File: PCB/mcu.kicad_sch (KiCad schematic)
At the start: 16 parts, among them J3 USB_A, SW1 SW_Push, SW2 SW_Push, SW3 SW_Push, SW4 SW_Push, U3 COM-09032, Y1 Crystal_GND24

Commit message: pls work
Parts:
- added C85, C86, C87, C88, C89, C90, C91: 100n, symbol Device:C
- added C92: 10u, symbol Device:C_Polarized_US
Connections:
- net +3.3V: now also C85.1, C86.1, C87.1, C88.1, C89.1, C90.1, C91.1, C92.1
- net GND: now also C85.2, C86.2, C87.2, C88.2, C89.2, C90.2, C91.2, C92.2

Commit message: Footprints
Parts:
- removed J3: USB_A, symbol Connector:USB_A
- added J6: USB1130-15-A_REVA, USB1130-15-A_REVA:GCT_USB1130-15-A_REVA, symbol USB1130-15-A_REVA:USB1130-15-A_REVA
- C20, C21, C22, C85, C86, C87, C88, C89, C90, C91, C92: footprint (none) -> Capacitor_SMD:C_0805_2012Metric_Pad1.18x1.45mm_HandSolder
- H1: footprint (none) -> efm32:QFP50P1200X1200X120-64N
- R10, R11, R12, R9: footprint (none) -> Resistor_SMD:R_0805_2012Metric_Pad1.20x1.40mm_HandSolder
- SW1, SW2, SW3, SW4: footprint (none) -> button:K12PBK15N
- U3: footprint COM-09032:XDCR_COM-09032 -> joystick:XDCR_COM-09032
- Y1: footprint (none) -> ECS-3953M-400-BN-TR:OSC_ECS-3953M-400-BN-TR
- renumbered DEBUG_HEADER to DEBUG_HEADER1
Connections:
- net 5V_IN: now also J6.1 (VCC)
- net GND: now also J6.4 (GND)
- net at H1.47 (PF10): now also J6.2 (D-)
- net at H1.48 (PF11): now also J6.3 (D+)
- new net: J6.S1 (SHIELD), J6.S2 (SHIELD)

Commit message: more
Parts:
- added R38, R39: 15, symbol Device:R
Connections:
- net +3.3VA is gone; now on net +3.3V: H1.23 (AVDD_1), H1.27 (AVDD_0)
- net 5V_IN: now also H1.52 (USB_VBUS)
- net GND: now also H1.33 (PD5), H1.34 (PD6), H1.35 (PD7), J6.S1 (SHIELD), J6.S2 (SHIELD), U3.S1 (SHIELD), U3.S2 (SHIELD), U3.S3 (SHIELD), U3.S4 (SHIELD); no longer H1.52 (USB_VBUS)
- net at J6.2 (D-): now also R38.2; no longer H1.47 (PF10)
- net at J6.3 (D+): now also R39.2; no longer H1.48 (PF11)
- net at DEBUG_HEADER1.12 (TRACECLK): no longer H1.35 (PD7)
- net at DEBUG_HEADER1.14 (TRACEDATA[0]): no longer H1.34 (PD6)
- net at DEBUG_HEADER1.16 (TRACEDATA[1]): no longer H1.31 (PD3)
- net at DEBUG_HEADER1.18 (TRACEDATA[2]): no longer H1.32 (PD4)
- net at DEBUG_HEADER1.20 (TRACEDATA[3]): no longer H1.33 (PD5)
- new net: H1.47 (PF10), R38.1
- new net: H1.48 (PF11), R39.1
- no-connect marks 6 -> 9

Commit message: schematic fixes
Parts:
- added C2: 10u?, Capacitor_SMD:C_0805_2012Metric_Pad1.18x1.45mm_HandSolder, symbol Device:C
- added C93: 1u, Capacitor_SMD:C_0805_2012Metric_Pad1.18x1.45mm_HandSolder, symbol Device:C
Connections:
- net 5V_IN: now also C2.1
- net GND: now also H1.31 (PD3), H1.32 (PD4), C2.2, C93.2; no longer H1.33 (PD5), H1.34 (PD6), H1.45 (USB_VREGI)
- net at H1.46 (USB_VREGO): now also H1.45 (USB_VREGI), C93.1
- new net done: H1.34 (PD6)
- new net program_b: H1.33 (PD5)
- no-connect marks 9 -> 8
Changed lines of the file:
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@@
   (junction (at 110.49 24.13) (diameter 0) (color 0 0 0 0)
   )
+  (junction (at 111.76 130.81) (diameter 0) (color 0 0 0 0)
+  )
   (junction (at 53.34 60.96) (diameter 0) (color 0 0 0 0)
   )
@@
   (junction (at 68.58 90.17) (diameter 0) (color 0 0 0 0)
   )
-  (junction (at 121.92 105.41) (diameter 0) (color 0 0 0 0)
+  (junction (at 121.92 77.47) (diameter 0) (color 0 0 0 0)
   )
   (junction (at 101.6 158.75) (diameter 0) (color 0 0 0 0)
@@
   (junction (at 118.745 31.75) (diameter 0) (color 0 0 0 0)
   )
+  (junction (at 128.905 80.01) (diameter 0) (color 0 0 0 0)
+  )
   (junction (at 127 31.75) (diameter 0) (color 0 0 0 0)
   )
@@
   (junction (at 57.15 60.96) (diameter 0) (color 0 0 0 0)
   )
-  (junction (at 121.92 107.95) (diameter 0) (color 0 0 0 0)
-  )
   (junction (at 49.53 74.93) (diameter 0) (color 0 0 0 0)
   )
@@
   )
   (junction (at 17.78 93.98) (diameter 0) (color 0 0 0 0)
+  )
+  (junction (at 139.7 41.91) (diameter 0) (color 0 0 0 0)
   )
   (junction (at 118.745 24.13) (diameter 0) (color 0 0 0 0)
@@
   (no_connect (at 125.73 162.56))
   (no_connect (at 201.93 90.17))
-  (no_connect (at 123.19 77.47))
   (no_connect (at 201.93 87.63))
   (no_connect (at 125.73 165.1))
   (no_connect (at 201.93 92.71))
+  (wire (pts (xy 142.875 80.01) (xy 147.32 80.01))
+    (stroke (width 0) (type default))
+  )
   (wire (pts (xy 88.9 158.75) (xy 91.44 158.75))
     (stroke (width 0) (type default))
@@
     (stroke (width 0) (type default))
   )
-  (wire (pts (xy 121.92 107.95) (xy 121.92 110.49))
-    (stroke (width 0) (type default))
-  )
   (wire (pts (xy 121.92 72.39) (xy 132.08 72.39))
     (stroke (width 0) (type default))
@@
     (stroke (width 0) (type default))
   )
-  (wire (pts (xy 111.76 130.81) (xy 111.76 133.35))
-    (stroke (width 0) (type default))
-  )
   (wire (pts (xy 36.83 80.01) (xy 36.83 114.3))
     (stroke (width 0) (type default))
   )
+  (wire (pts (xy 109.22 130.81) (xy 111.76 130.81))
+    (stroke (width 0) (type default))
+  )
   (wire (pts (xy 88.9 158.75) (xy 88.9 162.56))
     (stroke (width 0) (type default))
@@
     (stroke (width 0) (type default))
   )
+  (wire (pts (xy 121.92 77.47) (xy 128.905 77.47))
+    (stroke (width 0) (type default))
+  )
   (wire (pts (xy 147.32 63.5) (xy 149.86 63.5))
     (stroke (width 0) (type default))
@@
     (stroke (width 0) (type default))
   )
-  (wire (pts (xy 114.3 130.81) (xy 205.74 130.81))
-    (stroke (width 0) (type default))
-  )
   (wire (pts (xy 132.08 72.39) (xy 132.08 66.04))
     (stroke (width 0) (type default))
@@
     (stroke (width 0) (type default))
   )
-  (wire (pts (xy 121.92 105.41) (xy 121.92 107.95))
-    (stroke (width 0) (type default))
-  )
   (wire (pts (xy 68.58 107.95) (xy 60.96 107.95))
     (stroke (width 0) (type default))
   )
+  (wire (pts (xy 111.76 130.81) (xy 111.76 133.985))
+    (stroke (width 0) (type default))
+  )
   (wire (pts (xy 88.9 170.18) (xy 95.25 170.18))
     (stroke (width 0) (type default))
@@
     (stroke (width 0) (type default))
   )
-  (wire (pts (xy 111.76 133.35) (xy 208.28 133.35))
-    (stroke (width 0) (type default))
-  )
   (wire (pts (xy 96.52 52.07) (xy 96.52 39.37))
     (stroke (width 0) (type default))
@@
     (stroke (width 0) (type default))
   )
+  (wire (pts (xy 128.905 80.01) (xy 135.255 80.01))
+    (stroke (width 0) (type default))
+  )
   (wire (pts (xy 45.72 72.39) (xy 68.58 72.39))
     (stroke (width 0) (type default))
@@
     (stroke (width 0) (type default))
   )
-  (wire (pts (xy 121.92 80.01) (xy 147.32 80.01))
+  (wire (pts (xy 121.92 80.01) (xy 128.905 80.01))
     (stroke (width 0) (type default))
   )
@@
     (stroke (width 0) (type default))
   )
-  (wire (pts (xy 123.19 77.47) (xy 121.92 77.47))
-    (stroke (width 0) (type default))
-  )
   (wire (pts (xy 130.81 96.52) (xy 121.92 96.52))
     (stroke (width 0) (type default))
@@
     (stroke (width 0) (type default))
   )
+  (wire (pts (xy 121.285 77.47) (xy 121.92 77.47))
+    (stroke (width 0) (type default))
+  )
+  (wire (pts (xy 151.765 41.91) (xy 157.48 41.91))
+    (stroke (width 0) (type default))
+  )
   (wire (pts (xy 121.92 74.93) (xy 138.43 74.93))
     (stroke (width 0) (type default))
@@
     (stroke (width 0) (type default))
   )
+  (wire (pts (xy 139.7 41.91) (xy 144.145 41.91))
+    (stroke (width 0) (type default))
+  )
   (wire (pts (xy 207.01 45.72) (xy 109.22 45.72))
     (stroke (width 0) (type default))
@@
   )
   (wire (pts (xy 139.7 60.96) (xy 149.86 60.96))
+    (stroke (width 0) (type default))
+  )
+  (wire (pts (xy 128.905 77.47) (xy 128.905 80.01))
+    (stroke (width 0) (type default))
+  )
+  (wire (pts (xy 111.76 130.81) (xy 114.3 130.81))
     (stroke (width 0) (type default))
   )
@@
     (effects (font (size 1.27 1.27)) (justify right))
   )
+  (hierarchical_label "done" (shape input) (at 121.92 107.95 0) (fields_autoplaced)
+    (effects (font (size 1.27 1.27)) (justify left))
+  )
   (hierarchical_label "GPIO4" (shape input) (at 86.36 52.07 90) (fields_autoplaced)
     (effects (font (size 1.27 1.27)) (justify left))
@@
   )
   (hierarchical_label "GPIO3" (shape input) (at 83.82 52.07 90) (fields_autoplaced)
+    (effects (font (size 1.27 1.27)) (justify left))
+  )
+  (hierarchical_label "program_b" (shape input) (at 121.92 110.49 0) (fields_autoplaced)
     (effects (font (size 1.27 1.27)) (justify left))
   )
@@
         (path "/aa113cd6-c3ac-4890-9a84-1ea195994408/6d6ebb76-19de-41e4-9a7d-528f4e5c1c0f"
           (reference "#PWR010") (unit 1)
+        )
+      )
+    )
+  )
+  (symbol (lib_id "power:GND") (at 157.48 41.91 90) (unit 1)
+    (in_bom yes) (on_board yes) (dnp no) (fields_autoplaced)
+    (property "Reference" "#PWR058" (at 163.83 41.91 0)
+      (effects (font (size 1.27 1.27)) hide)
+    )
+    (property "Value" "GND" (at 160.655 41.91 90)
+      (effects (font (size 1.27 1.27)) (justify right))
+    )
+    (property "Footprint" "" (at 157.48 41.91 0)
+      (effects (font (size 1.27 1.27)) hide)
+    )
+    (property "Datasheet" "" (at 157.48 41.91 0)
+      (effects (font (size 1.27 1.27)) hide)
+    )
+    (pin "1")
+    (instances
+      (project "PCB"
+        (path "/aa113cd6-c3ac-4890-9a84-1ea195994408/6d6ebb76-19de-41e4-9a7d-528f4e5c1c0f"
+          (reference "#PWR058") (unit 1)
         )
       )
@@
     )
   )
+  (symbol (lib_id "Device:C") (at 147.955 41.91 90) (unit 1)
+    (in_bom yes) (on_board yes) (dnp no)
+    (property "Reference" "C2" (at 145.415 40.64 0)
+      (effects (font (size 1.27 1.27)) (justify left))
+    )
+    (property "Value" "10u?" (at 150.495 41.91 0)
+      (effects (font (size 1.27 1.27)) (justify left))
+    )
+    (property "Footprint" "Capacitor_SMD:C_0805_2012Metric_Pad1.18x1.45mm_HandSolder" (at 151.765 40.9448 0)
+      (effects (font (size 1.27 1.27)) hide)
+    )
+    (property "Datasheet" "~" (at 147.955 41.91 0)
+      (effects (font (size 1.27 1.27)) hide)
+    )
+    (pin "1")
+    (pin "2")
+    (instances
+      (project "PCB"
+        (path "/aa113cd6-c3ac-4890-9a84-1ea195994408"
+          (reference "C2") (unit 1)
+        )
+        (path "/aa113cd6-c3ac-4890-9a84-1ea195994408/854a1da6-0a91-483b-964f-5f1aec25ba6d"
+          (reference "C3") (unit 1)
+        )
+        (path "/aa113cd6-c3ac-4890-9a84-1ea195994408/6d6ebb76-19de-41e4-9a7d-528f4e5c1c0f"
+          (reference "C94") (unit 1)
+        )
+      )
+    )
+  )
   (symbol (lib_id "Device:R") (at 57.15 64.77 0) (unit 1)
     (in_bom yes) (on_board yes) (dnp no)
@@
     )
   )
-  (symbol (lib_id "power:GND") (at 109.22 130.81 0) (unit 1)
-    (in_bom yes) (on_board yes) (dnp no) (fields_autoplaced)
-    (property "Reference" "#PWR063" (at 109.22 137.16 0)
-      (effects (font (size 1.27 1.27)) hide)
-    )
-    (property "Value" "GND" (at 109.22 135.89 0)
-      (effects (font (size 1.27 1.27)))
-    )
-    (property "Footprint" "" (at 109.22 130.81 0)
-      (effects (font (size 1.27 1.27)) hide)
-    )
-    (property "Datasheet" "" (at 109.22 130.81 0)
+  (symbol (lib_id "power:GND") (at 111.76 133.985 0) (unit 1)
+    (in_bom yes) (on_board yes) (dnp no) (fields_autoplaced)
+    (property "Reference" "#PWR063" (at 111.76 140.335 0)
+      (effects (font (size 1.27 1.27)) hide)
+    )
+    (property "Value" "GND" (at 111.76 139.065 0)
+      (effects (font (size 1.27 1.27)))
+    )
+    (property "Footprint" "" (at 111.76 133.985 0)
+      (effects (font (size 1.27 1.27)) hide)
+    )
+    (property "Datasheet" "" (at 111.76 133.985 0)
       (effects (font (size 1.27 1.27)) hide)
     )
@@
         )
       )
+    )
+  )
+  (symbol (lib_id "Device:C") (at 139.065 80.01 90) (unit 1)
+    (in_bom yes) (on_board yes) (dnp no)
+    (property "Reference" "C93" (at 140.335 76.2 90)
+      (effects (font (size 1.27 1.27)))
+    )
+    (property "Value" "1u" (at 140.335 83.82 90)
+      (effects (font (size 1.27 1.27)))
+    )
+    (property "Footprint" "Capacitor_SMD:C_0805_2012Metric_Pad1.18x1.45mm_HandSolder" (at 142.875 79.0448 0)
+      (effects (font (size 1.27 1.27)) hide)
+    )
+    (property "Datasheet" "~" (at 139.065 80.01 0)
+      (effects (font (size 1.27 1.27)) hide)
+    )
+    (pin "1")
+    (pin "2")
+    (instances
+      (project "PCB"
+        (path "/aa113cd6-c3ac-4890-9a84-1ea195994408/6d6ebb76-19de-41e4-9a7d-528f4e5c1c0f"
+          (reference "C93") (unit 1)
+        )
+      )

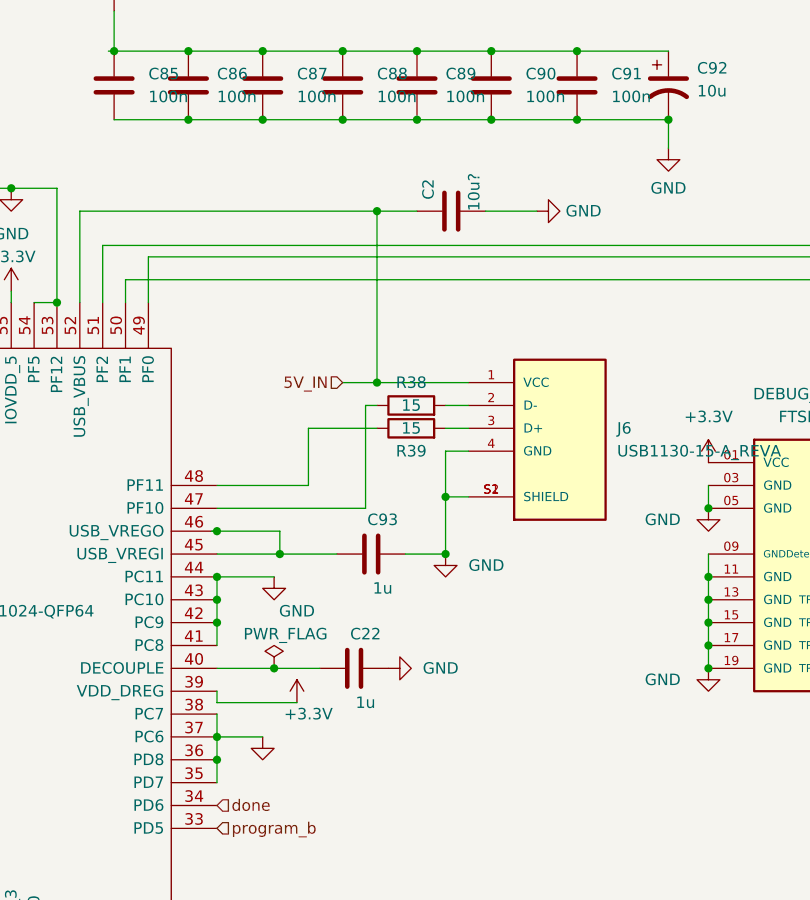
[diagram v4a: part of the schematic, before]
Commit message: schematic fixes.2
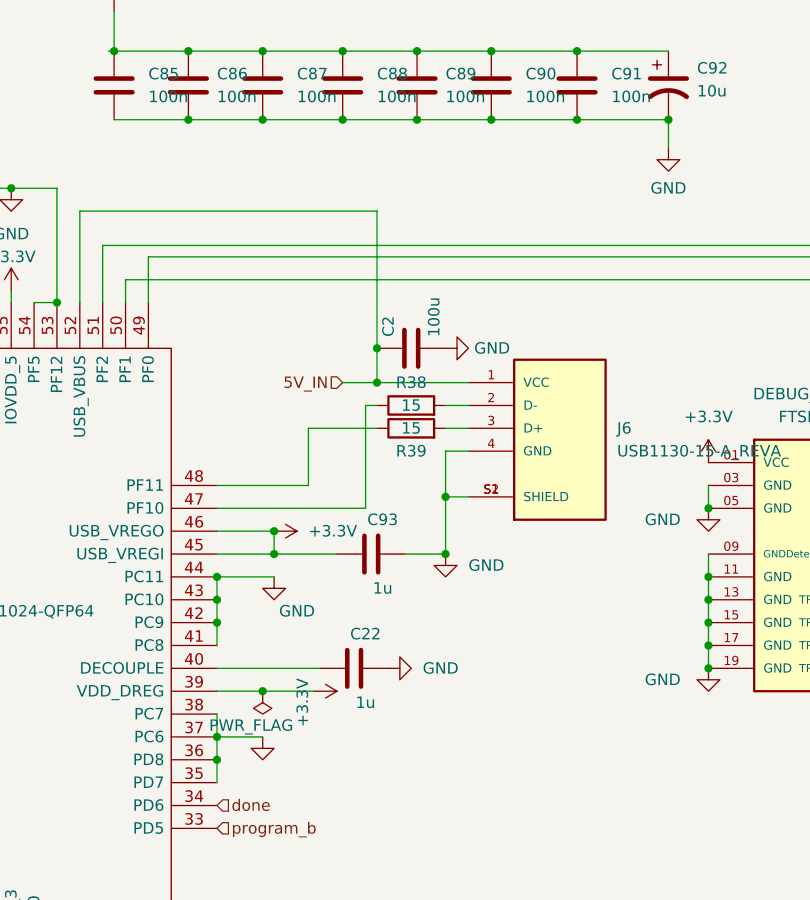
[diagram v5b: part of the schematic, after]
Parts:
- C2: value 10u? -> 100u
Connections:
- net +3.3V: now also C93.1, H1.45 (USB_VREGI), H1.46 (USB_VREGO)
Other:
- moved on the sheet: C2

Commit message: PCB
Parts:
- R38, R39: footprint (none) -> Resistor_SMD:R_0805_2012Metric_Pad1.20x1.40mm_HandSolder
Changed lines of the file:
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@@
       (effects (font (size 1.27 1.27)))
     )
-    (property "Footprint" "" (at 143.51 65.278 90)
+    (property "Footprint" "Resistor_SMD:R_0805_2012Metric_Pad1.20x1.40mm_HandSolder" (at 143.51 65.278 90)
       (effects (font (size 1.27 1.27)) hide)
     )
@@
       (effects (font (size 1.27 1.27)))
     )
-    (property "Footprint" "" (at 143.51 67.818 90)
-      (effects (font (size 1.27 1.27)) hide)
-    )
+    (property "Footprint" "Resistor_SMD:R_0805_2012Metric_Pad1.20x1.40mm_HandSolder" (at 143.51 67.818 90)
+      (effects (font (size 1.27 1.27)) hide)
+    )

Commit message: Finish PCB
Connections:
- net D1-: now reaches J6.2 (D-), R38.2
- net D1+: now reaches J6.3 (D+), R39.2
- net D-: now reaches H1.47 (PF10), R38.1
- net D+: now reaches H1.48 (PF11), R39.1
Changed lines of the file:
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@@
     (stroke (width 0) (type default))
+  )
+  (label "D1+" (at 148.59 66.04 0) (fields_autoplaced)
+    (effects (font (size 1.27 1.27)) (justify left bottom))
+  )
+  (label "D1-" (at 148.59 63.5 0) (fields_autoplaced)
+    (effects (font (size 1.27 1.27)) (justify left bottom))
+  )
+  (label "D-" (at 134.62 74.93 0) (fields_autoplaced)
+    (effects (font (size 1.27 1.27)) (justify left bottom))
+  )
+  (label "D+" (at 134.62 66.04 0) (fields_autoplaced)
+    (effects (font (size 1.27 1.27)) (justify left bottom))
   )
   (hierarchical_label "MISO" (shape input) (at 59.69 95.25 180) (fields_autoplaced)
